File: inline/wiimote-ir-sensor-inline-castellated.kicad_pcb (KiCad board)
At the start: 2 copper layers, 13 x 16 mm, 10 parts, among them J1 Conn_01x04_Pin, U2 AP2112-3.3V, X1 SG3225CAN 24.0000M-TJGA3

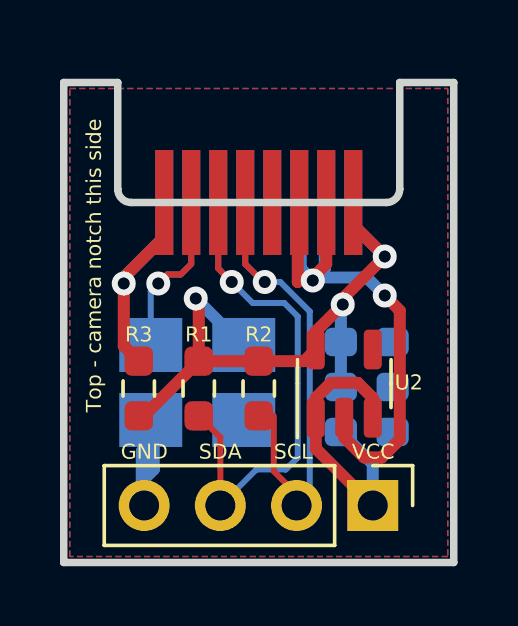
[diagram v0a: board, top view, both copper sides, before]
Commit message: Rev2 (#1)
Revision 2.

- Reroute to leave more empty space on sides
- Tweak camera footprint
- Add castellated variant
- Add manually panelised boards to help prevent panel tabs
  from appearing in edge connector
- Update readme
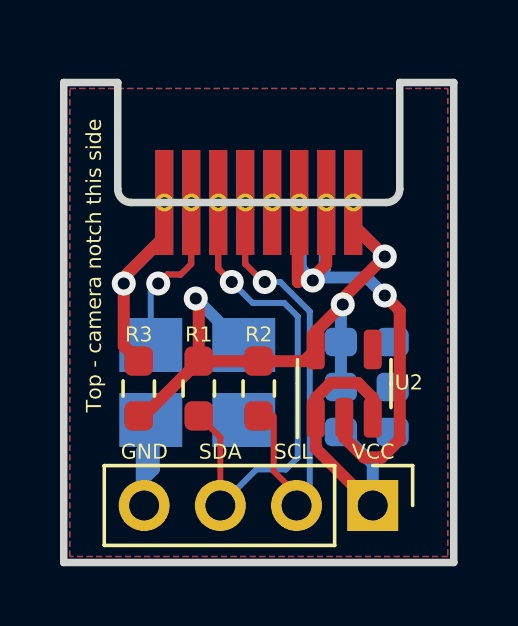
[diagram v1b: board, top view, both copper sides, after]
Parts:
- U1: footprint GUN4IR:wiimote-pixart-camera-inline -> GUN4IR:wiimote-pixart-camera-inline-castellated
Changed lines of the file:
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@@
 		)
 	)
-	(footprint "GUN4IR:wiimote-pixart-camera-inline"
+	(footprint "GUN4IR:wiimote-pixart-camera-inline-castellated"
 		(layer "B.Cu")
 		(at 106.5 101.5 180)
 		(property "Reference" "U1"
-			(at -5.4 -0.9 0)
+			(at 0.2 -5.3 0)
 			(unlocked yes)
 			(layer "B.SilkS")
 			(effects
 				(font
-					(size 0.5 0.5)
-					(thickness 0.08)
+					(size 1 1)
+					(thickness 0.15)
 				)
 				(justify mirror)
@@
 		)
 		(property "Footprint" ""
-			(at 0 0 180)
-			(unlocked yes)
-			(layer "F.Fab")
+			(at 0 0 0)
+			(unlocked yes)
+			(layer "B.Fab")
 			(hide yes)
 			(effects
@@
 					(size 1.27 1.27)
 				)
+				(justify mirror)
 			)
 		)
 		(property "Datasheet" ""
-			(at 0 0 180)
-			(unlocked yes)
-			(layer "F.Fab")
+			(at 0 0 0)
+			(unlocked yes)
+			(layer "B.Fab")
 			(hide yes)
 			(effects
@@
 					(size 1.27 1.27)
 				)
+				(justify mirror)
 			)
 		)
 		(property "Description" ""
-			(at 0 0 180)
-			(unlocked yes)
-			(layer "F.Fab")
+			(at 0 0 0)
+			(unlocked yes)
+			(layer "B.Fab")
 			(hide yes)
 			(effects
@@
 					(size 1.27 1.27)
 				)
-			)
-		)
-		(sheetfile "wiimote-ir-sensor-inline.kicad_sch")
+				(justify mirror)
+			)
+		)
 		(attr through_hole)
 		(fp_line
-			(start 4.7 1.5)
-			(end 4.7 -2.05)
+			(start 4.7 -2.05)
+			(end 4.7 1.5)
 			(stroke
 				(width 0.25)
@@
 		)
 		(fp_line
-			(start 4.25 -2.5)
-			(end -4.25 -2.5)
+			(start -4.25 -2.5)
+			(end 4.25 -2.5)
 			(stroke
 				(width 0.25)
@@
 		)
 		(fp_line
-			(start -4.7 1.5)
-			(end -4.7 -2.05)
+			(start -4.7 -2.05)
+			(end -4.7 1.5)
 			(stroke
 				(width 0.25)
@@
 		)
 		(fp_rect
-			(start -4.9 1.555)
-			(end 4.9 -2.645)
+			(start 4.9 -2.645)
+			(end -4.9 1.555)
 			(stroke
 				(width 0.05)
@@
 		)
 		(fp_rect
-			(start -4.9 1.555)
-			(end 4.9 -2.645)
+			(start 4.9 -2.645)
+			(end -4.9 1.555)
 			(stroke
 				(width 0.05)
@@
 			)
 		)
+		(pad "1" thru_hole circle
+			(at -3.15 -2.5 180)
+			(size 0.6 0.6)
+			(drill 0.346)
+			(layers "*.Cu" "*.Mask")
+			(remove_unused_layers no)
+			(net 1 "+3.3V")
+			(pinfunction "VCC")
+			(pintype "power_in")
+		)
 		(pad "1" smd rect
 			(at -3.15 -2.5 180)
@@
 			(pintype "power_in")
 		)
+		(pad "2" thru_hole circle
+			(at -2.25 -2.5 180)
+			(size 0.6 0.6)
+			(drill 0.346)
+			(layers "*.Cu" "*.Mask")
+			(remove_unused_layers no)
+			(net 2 "GND")
+			(pinfunction "GND")
+			(pintype "power_in")
+			(zone_connect 0)
+		)
 		(pad "2" smd rect
 			(at -2.25 -2.5 180)
@@
 			(zone_connect 0)
 		)
+		(pad "3" thru_hole circle
+			(at -1.35 -2.5 180)
+			(size 0.6 0.6)
+			(drill 0.346)
+			(layers "*.Cu" "*.Mask")
+			(remove_unused_layers no)
+			(net 2 "GND")
+			(pinfunction "GND")
+			(pintype "power_in")
+			(zone_connect 0)
+		)
 		(pad "3" smd rect
 			(at -1.35 -2.5 180)
@@
 			(zone_connect 0)
 		)
-		(pad "4" smd rect
+		(pad "4" thru_hole circle
 			(at -0.45 -2.5 180)
-			(size 0.6 3.5)
-			(layers "F.Cu" "F.Paste" "F.Mask")
+			(size 0.6 0.6)
+			(drill 0.346)
+			(layers "*.Cu" "*.Mask")
+			(remove_unused_layers no)
 			(net 7 "unconnected-(U1-NC-Pad4)")
 			(pinfunction "NC")
@@
 			(at -0.45 -2.5 180)
 			(size 0.6 3.5)
-			(layers "B.Cu" "B.Paste" "B.Mask")
+			(layers "F.Cu" "F.Paste" "F.Mask")
 			(net 7 "unconnected-(U1-NC-Pad4)")
 			(pinfunction "NC")
 			(pintype "no_connect")
 		)
+		(pad "4" smd rect
+			(at -0.45 -2.5 180)
+			(size 0.6 3.5)
+			(layers "B.Cu" "B.Paste" "B.Mask")
+			(net 7 "unconnected-(U1-NC-Pad4)")
+			(pinfunction "NC")
+			(pintype "no_connect")
+		)
+		(pad "5" thru_hole circle
+			(at 0.45 -2.5 180)
+			(size 0.6 0.6)
+			(drill 0.346)
+			(layers "*.Cu" "*.Mask")
+			(remove_unused_layers no)
+			(net 5 "/SCL")
+			(pinfunction "SCL")
+			(pintype "bidirectional")
+		)
 		(pad "5" smd rect
 			(at 0.45 -2.5 180)
@@
 			(pintype "bidirectional")
 		)
+		(pad "6" thru_hole circle
+			(at 1.35 -2.5 180)
+			(size 0.6 0.6)
+			(drill 0.346)
+			(layers "*.Cu" "*.Mask")
+			(remove_unused_layers no)
+			(net 4 "/SDA")
+			(pinfunction "SDA")
+			(pintype "bidirectional")
+		)
 		(pad "6" smd rect
 			(at 1.35 -2.5 180)
@@
 			(pintype "bidirectional")
 		)
+		(pad "7" thru_hole circle
+			(at 2.25 -2.5 180)
+			(size 0.6 0.6)
+			(drill 0.346)
+			(layers "*.Cu" "*.Mask")
+			(remove_unused_layers no)
+			(net 8 "/CLK")
+			(pinfunction "CLK")
+			(pintype "bidirectional")
+		)
 		(pad "7" smd rect
 			(at 2.25 -2.5 180)
@@
 			(pintype "bidirectional")
 		)
+		(pad "8" thru_hole circle
+			(at 3.15 -2.5 180)
+			(size 0.6 0.6)
+			(drill 0.346)
+			(layers "*.Cu" "*.Mask")
+			(remove_unused_layers no)
+			(net 6 "Net-(U1-RESET)")
+			(pinfunction "RESET")
+			(pintype "bidirectional")
+		)
